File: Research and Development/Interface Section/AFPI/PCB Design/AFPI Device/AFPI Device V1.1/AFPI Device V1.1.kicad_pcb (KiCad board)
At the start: 2 copper layers, 85 x 45 mm, 32 parts, among them J1 Batt I, J2 OLED, J3 ROT ENC, J4 RGB O, J5 HP O, J6 SP O, J7 AU O, J8 LINE I/PKP V, J9 BACK I, Q1 MPF102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

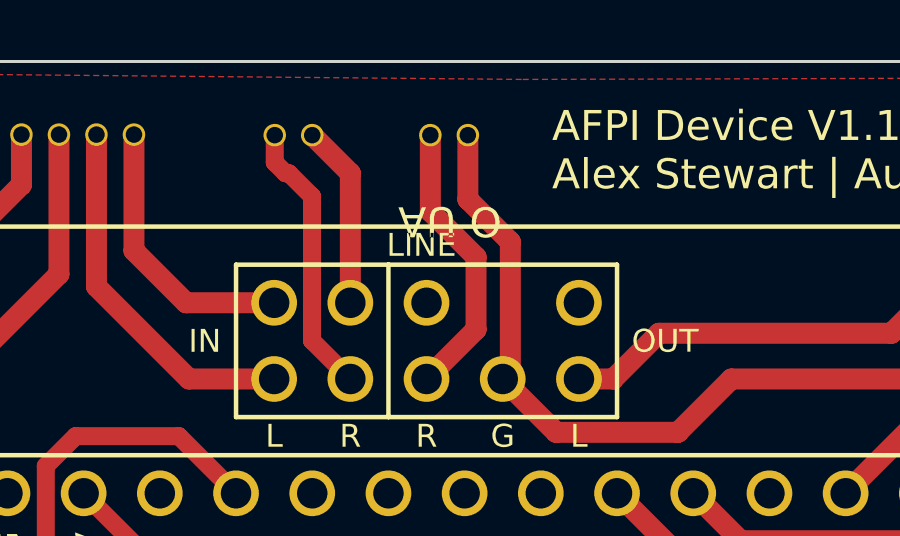
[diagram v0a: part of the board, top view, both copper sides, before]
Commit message: Completed First Revision of AFPI design and Assembly
Finished the initial design and g code generation of the top and bottom plates of the AFPI as well as the central enclosure. couldnt make gcode to fillet the exterior and interior edges as seen on the 3d model as the initial path tools werent enought to do it and i decided on a time scale that the filleted edges werent neccesary for now. if i deem them to be important when designing the guitar body, ill manually dremel fillets and chamfers, however this is not an ideal plan as acrylic is so damn temperamental and brittle.

Currently all packages for the AFPI have arrived and ive already produced the Top and Bottom plates. i took 2 takes for the top plate because the first attempts g code path for the holes used a pocket path which for some reason made the wholes too small. the 7.5mm holes were 6.5, the 3mm were 2.5 and the 2.5mm were ~2.1. when this happened i made the mistake of trying to redrill the holes and i cracked the plate in half on the second hole drilling (there were 16 holes i didnt get very far) on top of this the holes werent accurate circles as the endmill bit would start a bit far out on the edge of each hole.

to remedy this situation i had 3 options,

One would be to file or dremel sand each hole to their correct size, which would be painfully slow and wouldnt actually fix the problem as i would lose much of the advantages that come with a cnc mill being less man hours, accuracy and overall just a more simplistic way of manuafacturing a multi face piece.

The second option would be to use a drill bit to actually drill the holes rather then an endmill bit boring its way in. this wasnt really an option as i didnt want to use specialist bits. even anyway the only 7.5mm bit i could find for a cnc machine was 50$ AUD so no way was i gonna do that for 5 holes, plus i woulld need a 6.5mm as well for the 6.5 hole. The time as well to change each bit and zero the Z probe for each one would just be so time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
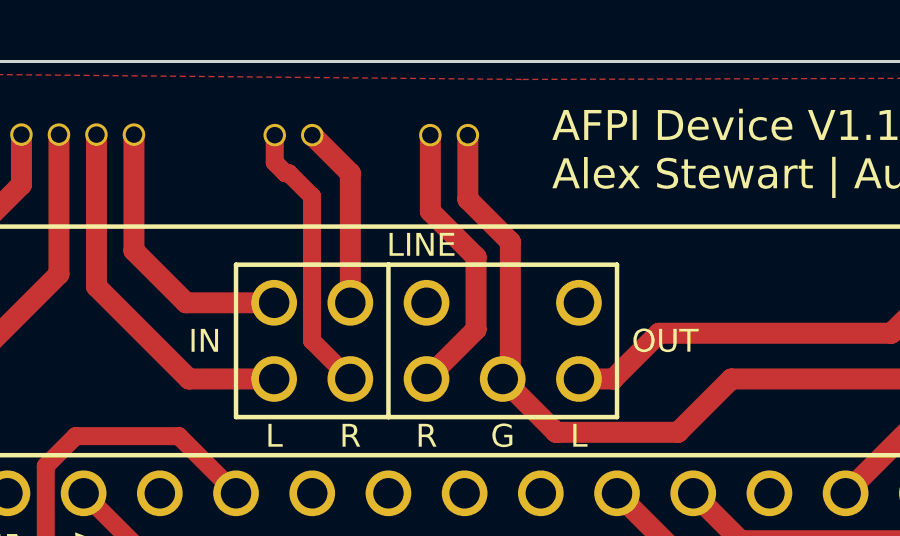
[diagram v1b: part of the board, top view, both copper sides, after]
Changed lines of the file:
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@@
     (pad_to_mask_clearance 0)
     (pcbplotparams
-      (layerselection 0x00010f0_7fffffff)
+      (layerselection 0x0000008_7ffffffe)
       (plot_on_all_layers_selection 0x0000000_00000000)
       (disableapertmacros false)
@@
       (drillshape 0)
       (scaleselection 1)
-      (outputdirectory "")
+      (outputdirectory "AFPI Gbr Files/")
     )
   )
@@
         (effects (font (size 1 1) (thickness 0.1)) (justify mirror))
     )
-    (fp_text value "AU O" (at 2.22 -0.818 180 unlocked) (layer "F.SilkS")
+    (fp_text value "AU O" (at 2.22 -0.818 180 unlocked) (layer "B.SilkS")
         (effects (font (size 1 1) (thickness 0.15)) (justify mirror))
     )

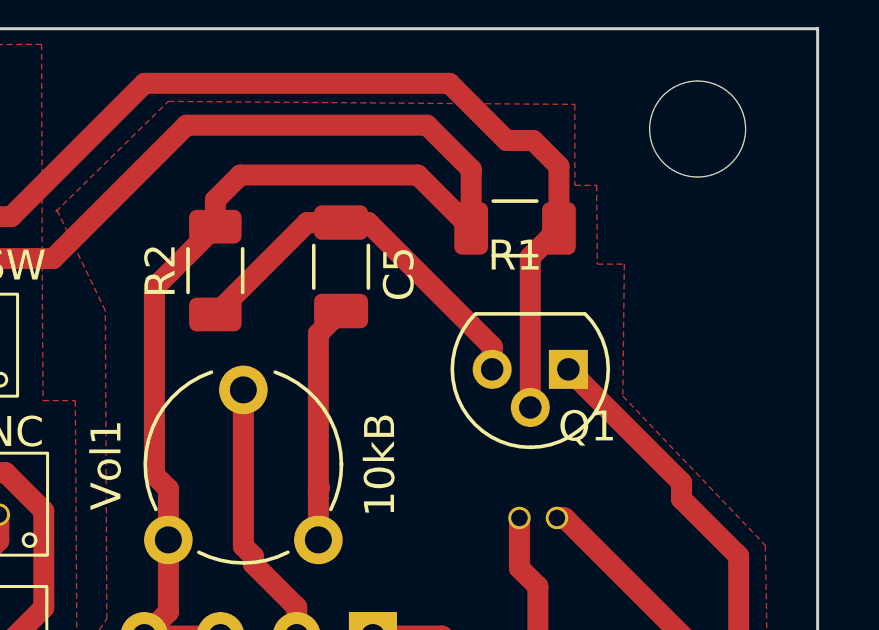
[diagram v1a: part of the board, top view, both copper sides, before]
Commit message: Solved Speaker Issue
After reviewing the pcb layout and the schematic, and reviewing each component, i noticed that the pin outs on the symbol for the MPF102 on the schem didnt number the pins correctly to their functions. while the drain pin was wired correctly, the gate and source pins were reversed, causing it to not work properly. this mistake occured because i used a standard n channel JFET symbol and a generic TO-92 package during the design phase as kikad didnt have the MPF102 in its libraries, sourcing one was challenging and i just decided to use the generic symbol as it was the same.

While i did check for the different pinouts as i was aware they vary from models, with the symbol displaying the same outputs as the ruby amp schematic in the right positions i thought the numbering was correct, and the pin table for the symbol was numbered 1, 2 and 3, the same as the components pins left to right, i overlooked however the fact that the numbers didnt correlate with their correct functions. Once it came to PCB design i didnt think about it much as afterall, i had gone over the schematic muiltiple times and the outputs matched original schematic, i also did the electrical rules checker on the schematic and on the pcb after i designed it, and both were fine, as this was overlooked.

 i carried on assuming it was correct but i always expected their to be an issue in the circuit and was prepared for that fact and read analysis's of the circuit online to understand how it should operate so i was able to trace the circuits components to identify how it operated. When i realised the pins on the physical circuit were funny thats when i realised the mistake, luckily so early in the circuit so i didnt have to go far, although i did check voltages on the LM386 to ensure it was getting voltages.

initially was worried that their was no ground from the power supply reaching the circuit as i hadnt connected a direct ground source to the amplifier and instead used a ground p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
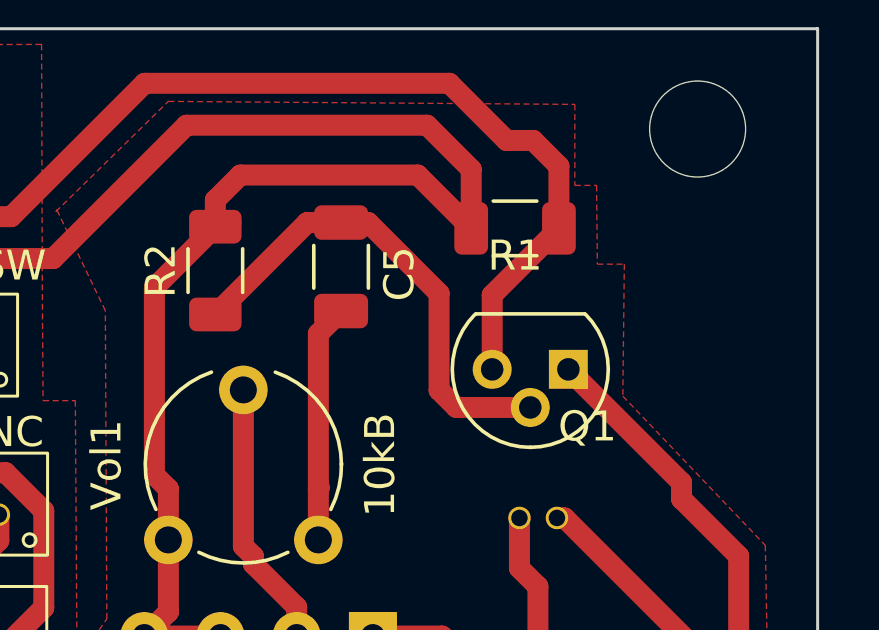
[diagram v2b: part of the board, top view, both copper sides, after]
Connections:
- Q1 pad 2: Net-(Q1-G) -> Net-(Q1-S)
- Q1 pad 3: Net-(Q1-S) -> Net-(Q1-G)
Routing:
- net Net-(Q1-S): track 13.0 -> 16.2 mm
- net Net-(Q1-G): track 54.7 -> 54.0 mm
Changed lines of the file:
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@@
       (net 1 "+9V") (pinfunction "D") (pintype "passive"))
     (pad "2" thru_hole circle (at 1.27 -1.27 180) (size 1.3 1.3) (drill 0.75) (layers "*.Cu" "*.Mask")
+      (net 48 "Net-(Q1-S)") (pinfunction "S") (pintype "passive"))
+    (pad "3" thru_hole circle (at 2.54 0 180) (size 1.3 1.3) (drill 0.75) (layers "*.Cu" "*.Mask")
       (net 47 "Net-(Q1-G)") (pinfunction "G") (pintype "input"))
-    (pad "3" thru_hole circle (at 2.54 0 180) (size 1.3 1.3) (drill 0.75) (layers "*.Cu" "*.Mask")
-      (net 48 "Net-(Q1-S)") (pinfunction "S") (pintype "passive"))
     (model "${KICAD6_3DMODEL_DIR}/Package_TO_SOT_THT.3dshapes/TO-92.wrl"
       (offset (xyz 0 0 0))
@@
   (segment (start 123.444 104.902) (end 123.083 104.541) (width 0.6) (layer "F.Cu") (net 46))
   (segment (start 124.325 105.672) (end 123.555 104.902) (width 0.6) (layer "F.Cu") (net 46))
-  (segment (start 174.7195 107.833) (end 173.765 108.7875) (width 0.7) (layer "F.Cu") (net 47))
-  (segment (start 173.765 108.7875) (end 173.765 113.802) (width 0.7) (layer "F.Cu") (net 47))
   (segment (start 173.863 104.902) (end 174.7195 105.7585) (width 0.7) (layer "F.Cu") (net 47))
   (segment (start 146.431 107.442) (end 156.464 107.442) (width 0.7) (layer "F.Cu") (net 47))
@@
   (segment (start 172.974 104.902) (end 173.863 104.902) (width 0.7) (layer "F.Cu") (net 47))
   (segment (start 171.069 102.997) (end 172.974 104.902) (width 0.7) (layer "F.Cu") (net 47))
-  (segment (start 172.495 111.77) (end 168.363 107.638) (width 0.7) (layer "F.Cu") (net 48))
-  (segment (start 172.495 112.532) (end 172.495 111.77) (width 0.7) (layer "F.Cu") (net 48))
+  (segment (start 172.495 110.0575) (end 172.495 112.532) (width 0.7) (layer "F.Cu") (net 47))
+  (segment (start 174.7195 107.833) (end 172.495 110.0575) (width 0.7) (layer "F.Cu") (net 47))
   (segment (start 166.3315 107.638) (end 163.267 110.7025) (width 0.7) (layer "F.Cu") (net 48))
   (segment (start 167.458 107.638) (end 166.3315 107.638) (width 0.7) (layer "F.Cu") (net 48))
-  (segment (start 168.363 107.638) (end 167.458 107.638) (width 0.7) (layer "F.Cu") (net 48))
+  (segment (start 167.458 107.638) (end 168.363 107.638) (width 0.7) (layer "F.Cu") (net 48))
+  (segment (start 170.725 110) (end 170.725 113.225) (width 0.7) (layer "F.Cu") (net 48))
+  (segment (start 168.363 107.638) (end 170.725 110) (width 0.7) (layer "F.Cu") (net 48))
+  (segment (start 171.302 113.802) (end 173.765 113.802) (width 0.7) (layer "F.Cu") (net 48))
+  (segment (start 170.725 113.225) (end 171.302 113.802) (width 0.7) (layer "F.Cu") (net 48))
   (segment (start 142.113 115.57) (end 144.399 113.284) (width 0.7) (layer "F.Cu") (net 49))
   (segment (start 152.591 113.284) (end 153.8 112.075) (width 0.7) (layer "F.Cu") (net 49))
